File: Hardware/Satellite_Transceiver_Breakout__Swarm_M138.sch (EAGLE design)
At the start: 60 parts, among them Q2 20V/4.2A/52mΩ/1.4W, Q4 20V/4.2A/52mΩ/1.4W, U1 CH340E_MSOP10, U2 SWARM_M138_TRANSCEIVER_MAIN, U3 3.3V

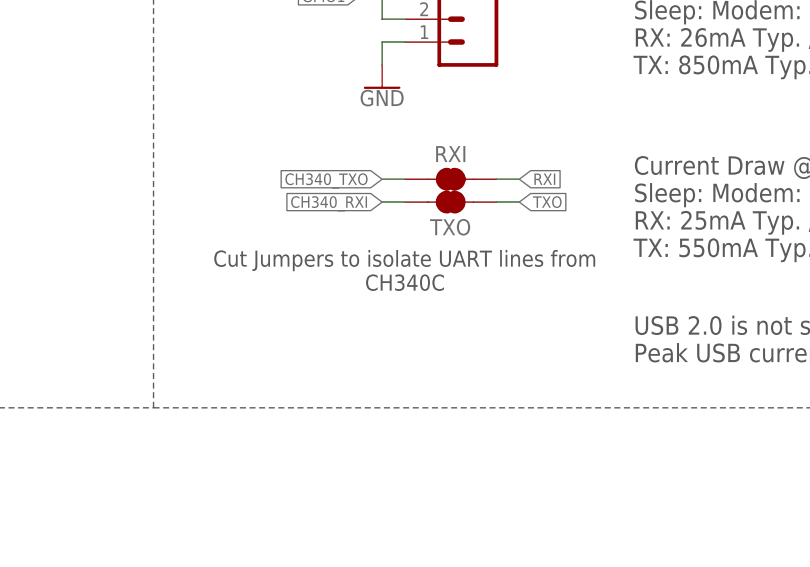
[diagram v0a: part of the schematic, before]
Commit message: Fixes small bit of text
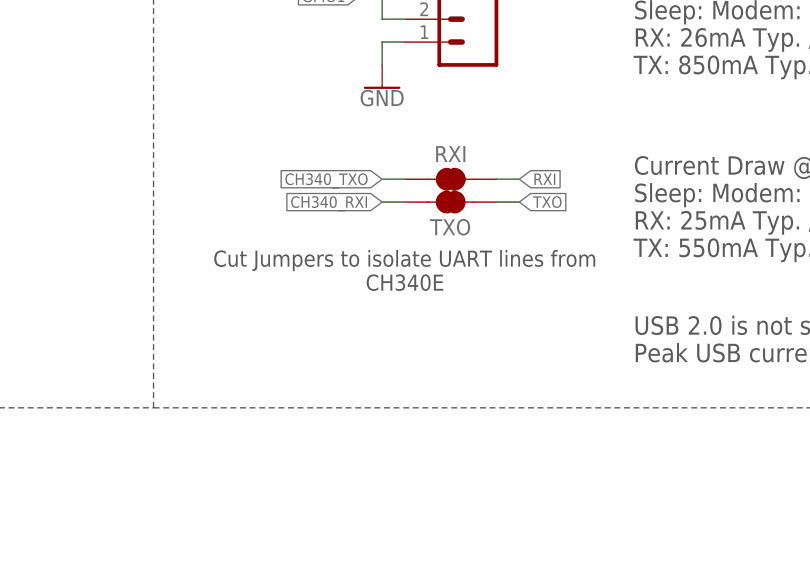
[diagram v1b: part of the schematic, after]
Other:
- note added: "Cut Jumpers to isolate UART lines from CH340E"
- note removed: "Cut Jumpers to isolate UART lines from CH340C"
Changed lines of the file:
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@@
 from ground.</text>
 <text x="340.36" y="129.54" size="1.778" layer="97" font="vector" align="center">Cut Jumpers to isolate UART lines from
-CH340C</text>
+CH340E</text>
 </plain>
 <instances>

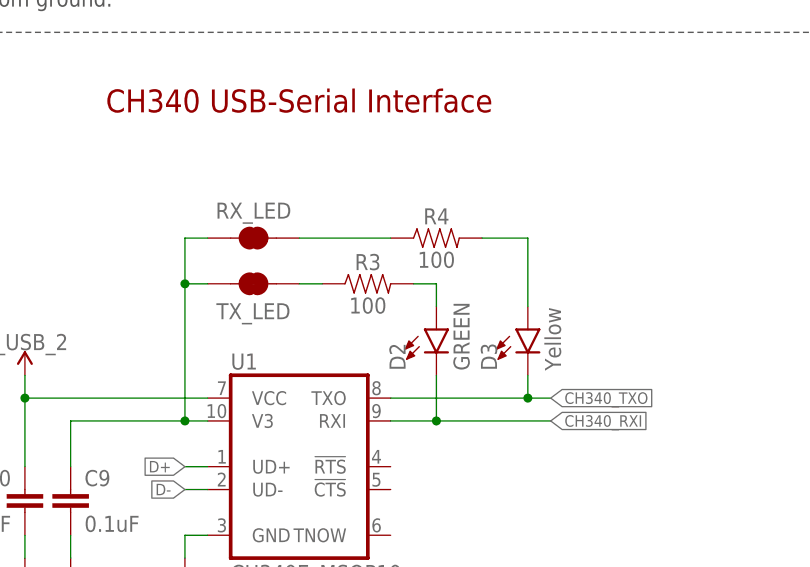
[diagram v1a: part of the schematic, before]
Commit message: Updates current limiting resistors for LEDs: 1k for green and 2.2K for yellow
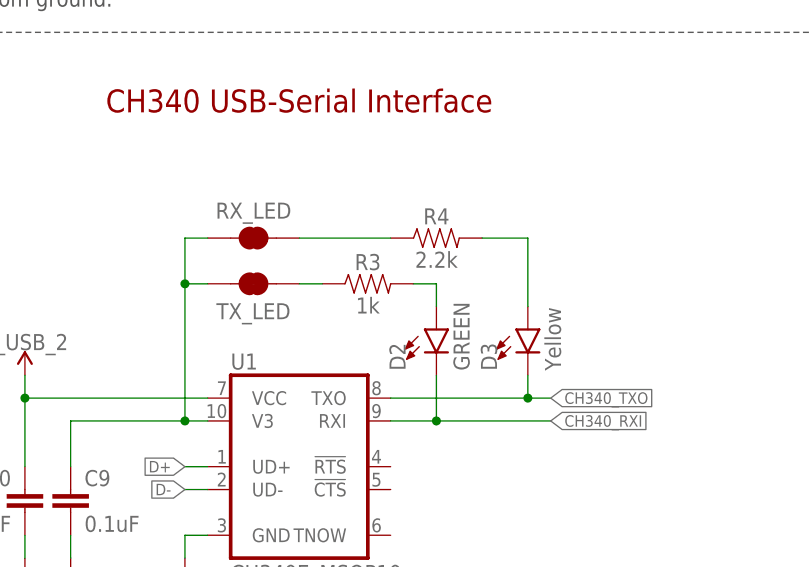
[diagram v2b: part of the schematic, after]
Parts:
- R3: value 100 -> 1k; device SparkFun-Resistors:100OHM-0603-1/10W-1% -> SparkFun-Resistors:1KOHM-0603-1/10W-1%
- R4: value 100 -> 2.2k; device SparkFun-Resistors:100OHM-0603-1/10W-1% -> SparkFun-Resistors:2.2KOHM-0603-1/10W-1%
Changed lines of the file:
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@@
 <part name="D2" library="SparkFun-LED" deviceset="LED-GREEN" device="0603" value="GREEN"/>
 <part name="D3" library="SparkFun-LED" deviceset="LED-YELLOW" device="0603" value="Yellow"/>
-<part name="R3" library="SparkFun-Resistors" deviceset="100OHM" device="-0603-1/10W-1%" value="100"/>
-<part name="R4" library="SparkFun-Resistors" deviceset="100OHM" device="-0603-1/10W-1%" value="100"/>
+<part name="R3" library="SparkFun-Resistors" deviceset="1KOHM" device="-0603-1/10W-1%" value="1k"/>
+<part name="R4" library="SparkFun-Resistors" deviceset="2.2KOHM" device="-0603-1/10W-1%" value="2.2k"/>
 <part name="RXI" library="SparkFun-Jumpers" deviceset="JUMPER-COMBO_2_NC_TRACE" device=""/>
 <part name="TXO" library="SparkFun-Jumpers" deviceset="JUMPER-COMBO_2_NC_TRACE" device=""/>
